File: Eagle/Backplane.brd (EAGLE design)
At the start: 190.2 x 38.1 mm, 14 parts

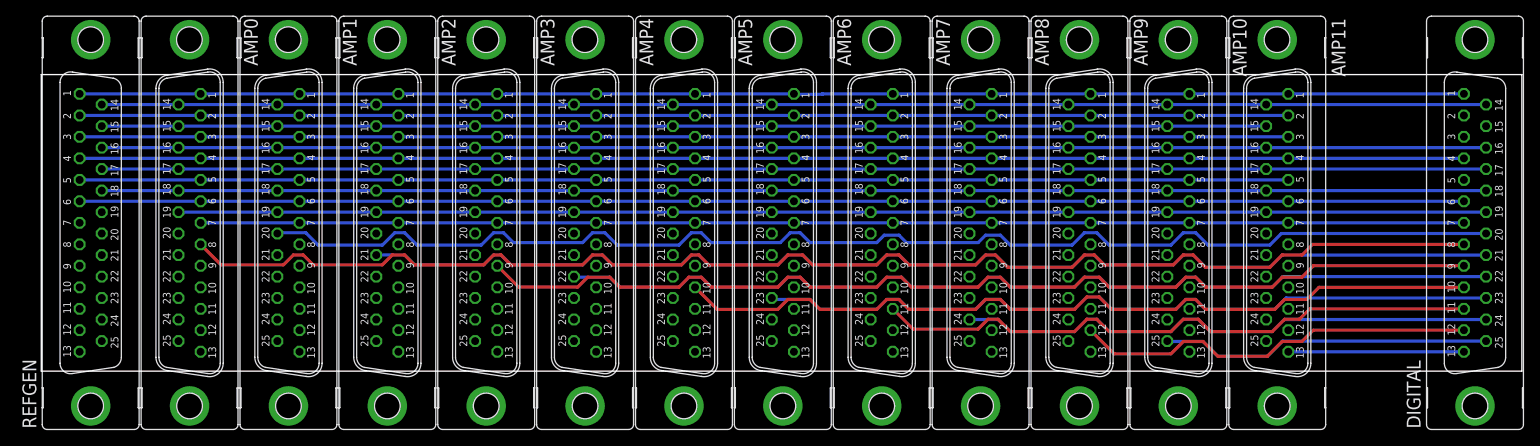
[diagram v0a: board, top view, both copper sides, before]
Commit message: Corrected connector positions
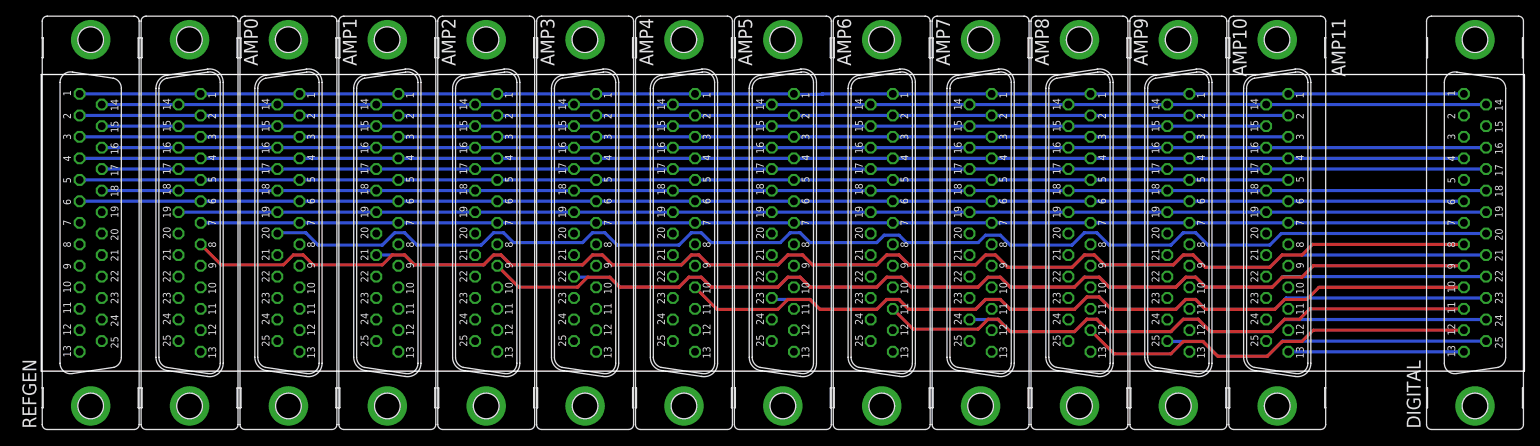
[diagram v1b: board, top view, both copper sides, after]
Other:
- board size 190.2 x 38.1 mm -> 190.5 x 38.1 mm
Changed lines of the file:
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@@
 <board>
 <plain>
-<wire x1="0" y1="10.16" x2="190.17" y2="10.16" width="0" layer="20"/>
-<wire x1="190.17" y1="10.16" x2="190.17" y2="48.25" width="0" layer="20"/>
-<wire x1="190.17" y1="48.25" x2="0" y2="48.25" width="0" layer="20"/>
-<wire x1="0" y1="48.25" x2="0" y2="10.16" width="0" layer="20"/>
+<wire x1="0" y1="10.16" x2="190.5" y2="10.16" width="0" layer="20"/>
+<wire x1="190.5" y1="10.16" x2="190.5" y2="48.26" width="0" layer="20"/>
+<wire x1="190.5" y1="48.26" x2="0" y2="48.26" width="0" layer="20"/>
+<wire x1="0" y1="48.26" x2="0" y2="10.16" width="0" layer="20"/>
 </plain>
 <attributes>
